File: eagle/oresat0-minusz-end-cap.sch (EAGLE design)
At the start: 30 parts, among them U1 LTC4305, U2 MMC5883MA, U3 MMC5883MA

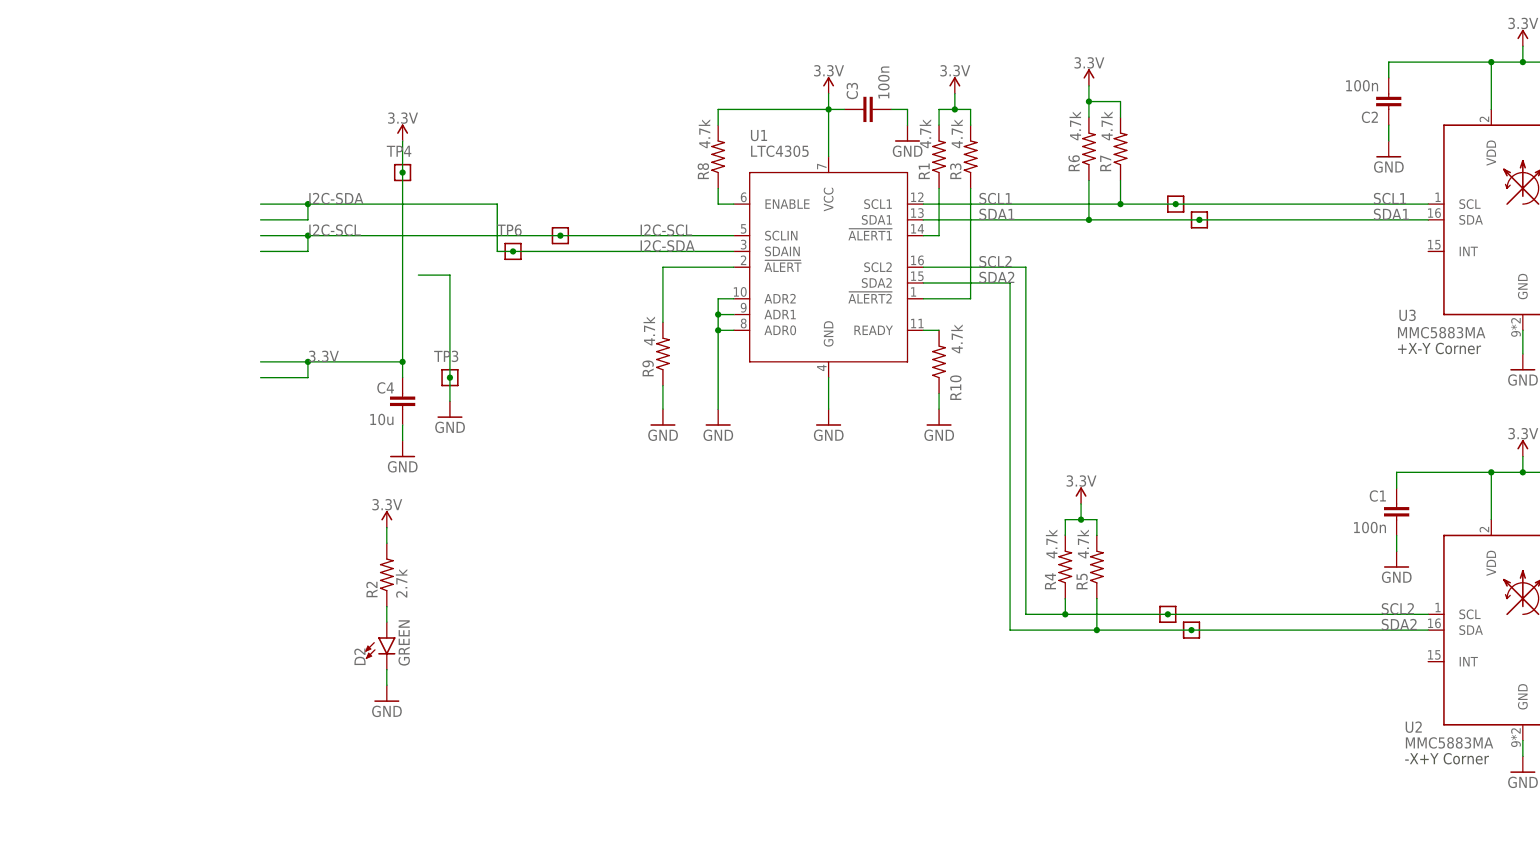
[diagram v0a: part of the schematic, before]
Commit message: Added connector to backplane. Added NP resistors connecting magnetometer interrupts to i2c buffer alert inputs. Moved traces out of bstop area, and moved components away from the backplane. Changed bus buffer i2c address. Added ground plane stitching, and fixed sharp edges on board outline.
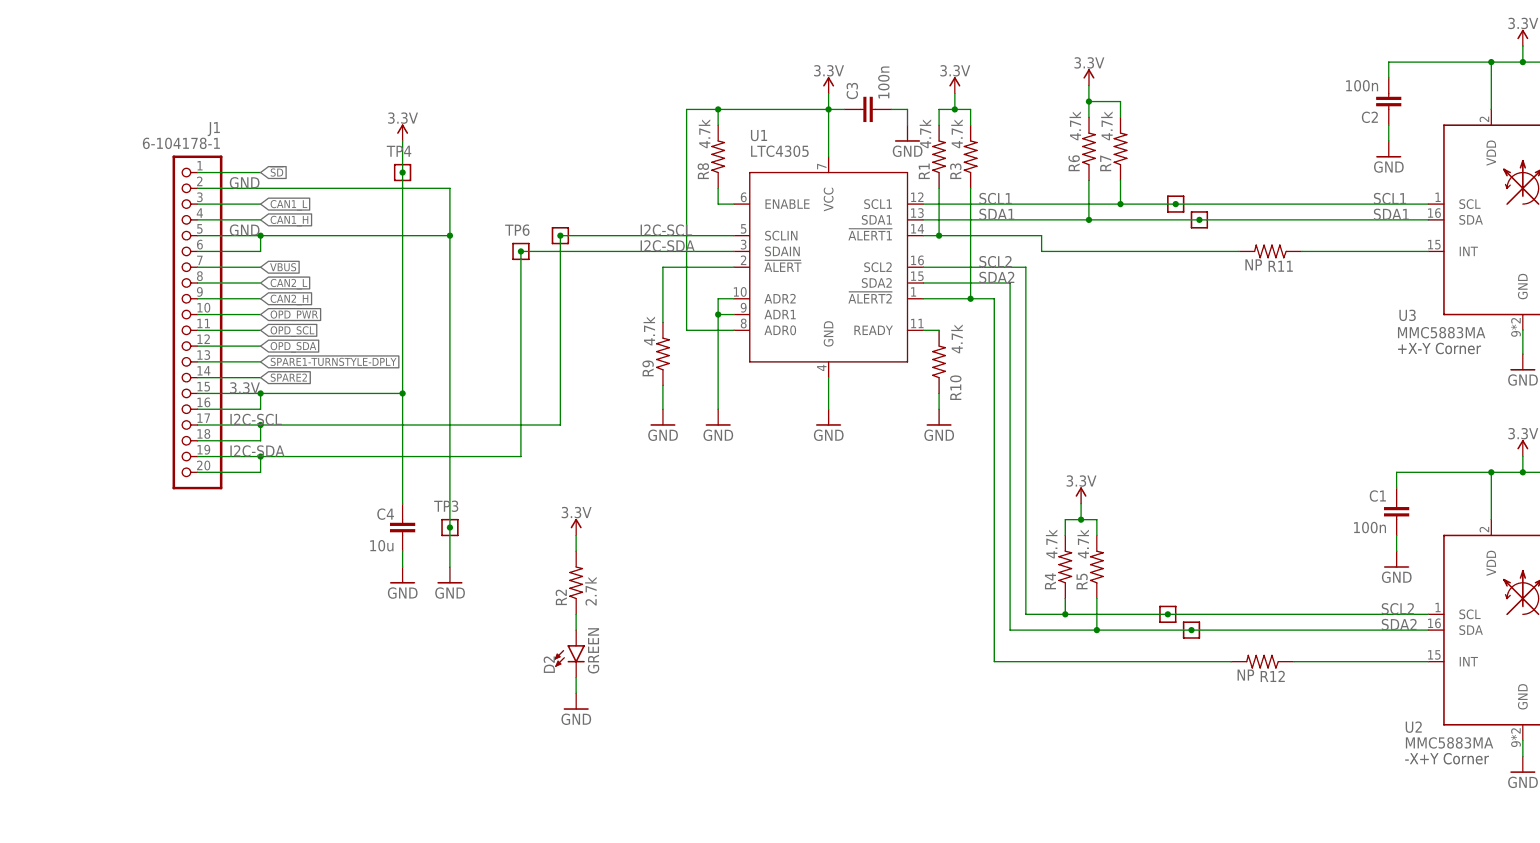
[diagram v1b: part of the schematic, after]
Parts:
- added J1: 6-104178-1, J-TE-6-104178-1-1.27mm-male-th:6-104178-1
- added R11, R12: NP, oresat-rcl:R-US_0603-B-NOSILK
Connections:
- new net !SD: J1.1
- new net CAN1_H: J1.4
- new net CAN1_L: J1.3
- new net CAN2_H: J1.9
- new net CAN2_L: J1.8
- new net N$10: R12.1, U2.INT
- new net N$8: R11.1, U3.INT
- new net OPD_PWR: J1.10
- new net OPD_SCL: J1.11
- new net OPD_SDA: J1.12
- new net SPARE1-TURNSTYLE-DPLY: J1.13
- new net SPARE2: J1.14
- new net VBUS: J1.7
- net 3.3V: now also J1.15, J1.16, U1.ADR0
- net GND: now also J1.2, J1.5, J1.6; no longer U1.ADR0
- net I2C-SCL: now also J1.17, J1.18
- net I2C-SDA: now also J1.19, J1.20
- net N$3: now also R11.2
- net N$4: now also R12.2
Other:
- moved on the sheet: C4, D2, R2, TP3, TP6

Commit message: v1.0 end caps for OreSat0!
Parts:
- added TP10, TP11, TP12, TP13, TP14, TP15, TP16, TP17, TP18, TP19, TP9: TEST-POINT-LARGE-SQUARE, oresat-misc:TEST-POINT-LARGE-SQUARE
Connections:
- net !SD: now also TP9.1
- net CAN1_H: now also TP11.1
- net CAN1_L: now also TP10.1
- net CAN2_H: now also TP14.1
- net CAN2_L: now also TP13.1
- net OPD_PWR: now also TP15.1
- net OPD_SCL: now also TP16.1
- net OPD_SDA: now also TP17.1
- net SPARE1-TURNSTYLE-DPLY: now also TP18.1
- net SPARE2: now also TP19.1
- net VBUS: now also TP12.1
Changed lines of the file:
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@@
 <?xml version="1.0" encoding="utf-8"?>
 <!DOCTYPE eagle SYSTEM "eagle.dtd">
-<eagle version="9.5.1">
+<eagle version="9.6.1">
 <drawing>
 <settings>
@@
 <setting verticaltext="up"/>
 </settings>
-<grid distance="0.05" unitdist="inch" unit="inch" style="lines" multiple="1" display="no" altdistance="0.01" altunitdist="inch" altunit="inch"/>
+<grid distance="0.1" unitdist="inch" unit="inch" style="lines" multiple="1" display="no" altdistance="0.01" altunitdist="inch" altunit="inch"/>
 <layers>
 <layer number="1" name="Top" color="4" fill="1" visible="no" active="no"/>
@@
 </part>
 <part name="J1" library="J-TE-6-104178-1-1.27mm-male-th" deviceset="6-104178-1" device=""/>
+<part name="TP9" library="oresat-misc" deviceset="TEST-POINT-LARGE-SQUARE" device=""/>
+<part name="TP10" library="oresat-misc" deviceset="TEST-POINT-LARGE-SQUARE" device=""/>
+<part name="TP11" library="oresat-misc" deviceset="TEST-POINT-LARGE-SQUARE" device=""/>
+<part name="TP12" library="oresat-misc" deviceset="TEST-POINT-LARGE-SQUARE" device=""/>
+<part name="TP13" library="oresat-misc" deviceset="TEST-POINT-LARGE-SQUARE" device=""/>
+<part name="TP14" library="oresat-misc" deviceset="TEST-POINT-LARGE-SQUARE" device=""/>
+<part name="TP15" library="oresat-misc" deviceset="TEST-POINT-LARGE-SQUARE" device=""/>
+<part name="TP16" library="oresat-misc" deviceset="TEST-POINT-LARGE-SQUARE" device=""/>
+<part name="TP17" library="oresat-misc" deviceset="TEST-POINT-LARGE-SQUARE" device=""/>
+<part name="TP18" library="oresat-misc" deviceset="TEST-POINT-LARGE-SQUARE" device=""/>
+<part name="TP19" library="oresat-misc" deviceset="TEST-POINT-LARGE-SQUARE" device=""/>
 </parts>
 <sheets>
@@
 <attribute name="VALUE" x="82.55" y="168.91" size="1.778" layer="96" rot="MR0"/>
 </instance>
+<instance part="TP9" gate="G$1" x="96.52" y="165.1" smashed="yes">
+<attribute name="NAME" x="99.06" y="165.1" size="1.27" layer="104"/>
+</instance>
+<instance part="TP10" gate="G$1" x="96.52" y="160.02" smashed="yes">
+<attribute name="NAME" x="99.06" y="160.02" size="1.27" layer="104"/>
+</instance>
+<instance part="TP11" gate="G$1" x="96.52" y="157.48" smashed="yes">
+<attribute name="NAME" x="99.06" y="157.48" size="1.27" layer="104"/>
+</instance>
+<instance part="TP12" gate="G$1" x="96.52" y="149.86" smashed="yes">
+<attribute name="NAME" x="99.06" y="149.86" size="1.27" layer="104"/>
+</instance>
+<instance part="TP13" gate="G$1" x="96.52" y="147.32" smashed="yes">
+<attribute name="NAME" x="99.06" y="147.32" size="1.27" layer="104"/>
+</instance>
+<instance part="TP14" gate="G$1" x="96.52" y="144.78" smashed="yes">
+<attribute name="NAME" x="99.06" y="144.78" size="1.27" layer="104"/>
+</instance>
+<instance part="TP15" gate="G$1" x="96.52" y="142.24" smashed="yes">
+<attribute name="NAME" x="99.06" y="142.24" size="1.27" layer="104"/>
+</instance>
+<instance part="TP16" gate="G$1" x="96.52" y="139.7" smashed="yes">
+<attribute name="NAME" x="99.06" y="139.7" size="1.27" layer="104"/>
+</instance>
+<instance part="TP17" gate="G$1" x="96.52" y="137.16" smashed="yes">
+<attribute name="NAME" x="99.06" y="137.16" size="1.27" layer="104"/>
+</instance>
+<instance part="TP18" gate="G$1" x="96.52" y="134.62" smashed="yes">
+<attribute name="NAME" x="99.06" y="134.62" size="1.27" layer="104"/>
+</instance>
+<instance part="TP19" gate="G$1" x="96.52" y="132.08" smashed="yes">
+<attribute name="NAME" x="99.06" y="132.08" size="1.27" layer="104"/>
+</instance>
 </instances>
 <busses>
@@
 <wire x1="78.74" y1="162.56" x2="119.38" y2="162.56" width="0.1524" layer="91"/>
 <pinref part="J1" gate="G$1" pin="5"/>
-<wire x1="78.74" y1="154.94" x2="88.9" y2="154.94" width="0.1524" layer="91"/>
+<wire x1="78.74" y1="154.94" x2="83.82" y2="154.94" width="0.1524" layer="91"/>
 <junction x="119.38" y="154.94"/>
 <pinref part="J1" gate="G$1" pin="6"/>
-<wire x1="88.9" y1="154.94" x2="119.38" y2="154.94" width="0.1524" layer="91"/>
-<wire x1="78.74" y1="152.4" x2="88.9" y2="152.4" width="0.1524" layer="91"/>
-<wire x1="88.9" y1="152.4" x2="88.9" y2="154.94" width="0.1524" layer="91"/>
-<junction x="88.9" y="154.94"/>
+<wire x1="83.82" y1="154.94" x2="119.38" y2="154.94" width="0.1524" layer="91"/>
+<wire x1="78.74" y1="152.4" x2="83.82" y2="152.4" width="0.1524" layer="91"/>
+<wire x1="83.82" y1="152.4" x2="83.82" y2="154.94" width="0.1524" layer="91"/>
+<junction x="83.82" y="154.94"/>
 <label x="83.82" y="162.56" size="1.778" layer="95"/>
 <label x="83.82" y="154.94" size="1.778" layer="95"/>
@@
 <segment>
 <pinref part="J1" gate="G$1" pin="1"/>
-<wire x1="78.74" y1="165.1" x2="88.9" y2="165.1" width="0.1524" layer="91"/>
-<label x="88.9" y="165.1" size="1.27" layer="95" xref="yes"/>
+<label x="83.82" y="165.1" size="1.27" layer="95"/>
+<pinref part="TP9" gate="G$1" pin="1"/>
+<wire x1="78.74" y1="165.1" x2="96.52" y2="165.1" width="0.1524" layer="91"/>
 </segment>
 </net>
@@
 <segment>
 <pinref part="J1" gate="G$1" pin="3"/>
-<wire x1="78.74" y1="160.02" x2="88.9" y2="160.02" width="0.1524" layer="91"/>
-<label x="88.9" y="160.02" size="1.27" layer="95" xref="yes"/>
+<label x="83.82" y="160.02" size="1.27" layer="95"/>
+<pinref part="TP10" gate="G$1" pin="1"/>
+<wire x1="78.74" y1="160.02" x2="96.52" y2="160.02" width="0.1524" layer="91"/>
 </segment>
 </net>
@@
 <segment>
 <pinref part="J1" gate="G$1" pin="4"/>
-<wire x1="78.74" y1="157.48" x2="88.9" y2="157.48" width="0.1524" layer="91"/>
-<label x="88.9" y="157.48" size="1.27" layer="95" xref="yes"/>
+<label x="83.82" y="157.48" size="1.27" layer="95"/>
+<pinref part="TP11" gate="G$1" pin="1"/>
+<wire x1="96.52" y1="157.48" x2="78.74" y2="157.48" width="0.1524" layer="91"/>
 </segment>
 </net>
@@
 <segment>
 <pinref part="J1" gate="G$1" pin="7"/>
-<wire x1="78.74" y1="149.86" x2="88.9" y2="149.86" width="0.1524" layer="91"/>
-<label x="88.9" y="149.86" size="1.27" layer="95" xref="yes"/>
+<label x="83.82" y="149.86" size="1.27" layer="95"/>
+<pinref part="TP12" gate="G$1" pin="1"/>
+<wire x1="78.74" y1="149.86" x2="96.52" y2="149.86" width="0.1524" layer="91"/>
 </segment>
 </net>
@@
 <segment>
 <pinref part="J1" gate="G$1" pin="8"/>
-<wire x1="78.74" y1="147.32" x2="88.9" y2="147.32" width="0.1524" layer="91"/>
-<label x="88.9" y="147.32" size="1.27" layer="95" xref="yes"/>
+<label x="83.82" y="147.32" size="1.27" layer="95"/>
+<pinref part="TP13" gate="G$1" pin="1"/>
+<wire x1="96.52" y1="147.32" x2="78.74" y2="147.32" width="0.1524" layer="91"/>
 </segment>
 </net>
@@
 <segment>
 <pinref part="J1" gate="G$1" pin="9"/>
-<wire x1="78.74" y1="144.78" x2="88.9" y2="144.78" width="0.1524" layer="91"/>
-<label x="88.9" y="144.78" size="1.27" layer="95" xref="yes"/>
+<label x="83.82" y="144.78" size="1.27" layer="95"/>
+<pinref part="TP14" gate="G$1" pin="1"/>
+<wire x1="78.74" y1="144.78" x2="96.52" y2="144.78" width="0.1524" layer="91"/>
 </segment>
 </net>
@@
 <segment>
 <pinref part="J1" gate="G$1" pin="10"/>
-<wire x1="78.74" y1="142.24" x2="88.9" y2="142.24" width="0.1524" layer="91"/>
-<label x="88.9" y="142.24" size="1.27" layer="95" xref="yes"/>
+<label x="83.82" y="142.24" size="1.27" layer="95"/>
+<pinref part="TP15" gate="G$1" pin="1"/>
+<wire x1="96.52" y1="142.24" x2="78.74" y2="142.24" width="0.1524" layer="91"/>
 </segment>
 </net>
@@
 <segment>
 <pinref part="J1" gate="G$1" pin="11"/>
-<wire x1="78.74" y1="139.7" x2="88.9" y2="139.7" width="0.1524" layer="91"/>
-<label x="88.9" y="139.7" size="1.27" layer="95" xref="yes"/>
+<label x="83.82" y="139.7" size="1.27" layer="95"/>
+<pinref part="TP16" gate="G$1" pin="1"/>
+<wire x1="78.74" y1="139.7" x2="96.52" y2="139.7" width="0.1524" layer="91"/>
 </segment>
 </net>
@@
 <segment>
 <pinref part="J1" gate="G$1" pin="12"/>
-<wire x1="78.74" y1="137.16" x2="88.9" y2="137.16" width="0.1524" layer="91"/>
-<label x="88.9" y="137.16" size="1.27" layer="95" xref="yes"/>
+<label x="83.82" y="137.16" size="1.27" layer="95"/>
+<pinref part="TP17" gate="G$1" pin="1"/>
+<wire x1="96.52" y1="137.16" x2="78.74" y2="137.16" width="0.1524" layer="91"/>
 </segment>
 </net>
@@
 <segment>
 <pinref part="J1" gate="G$1" pin="13"/>
-<wire x1="78.74" y1="134.62" x2="88.9" y2="134.62" width="0.1524" layer="91"/>
-<label x="88.9" y="134.62" size="1.27" layer="95" xref="yes"/>
+<label x="83.82" y="134.62" size="1.27" layer="95"/>
+<pinref part="TP18" gate="G$1" pin="1"/>
+<wire x1="78.74" y1="134.62" x2="96.52" y2="134.62" width="0.1524" layer="91"/>
 </segment>
 </net>
@@
 <segment>
 <pinref part="J1" gate="G$1" pin="14"/>
-<wire x1="78.74" y1="132.08" x2="88.9" y2="132.08" width="0.1524" layer="91"/>
-<label x="88.9" y="132.08" size="1.27" layer="95" xref="yes"/>
-</segment>
-</net>
+<label x="83.82" y="132.08" size="1.27" layer="95"/>
+<pinref part="TP19" gate="G$1" pin="1"/>
+<wire x1="96.52" y1="132.08" x2="78.74" y2="132.08" width="0.1524" layer="91"/>
+</segment>
+</net>

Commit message: Added BOMs and updated attributes for OreSat0 + and - Z end caps.
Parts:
- C1, C10, C2, C3, C7: DPN 1276-1001-1-ND -> 1276-CL10B104KB8NNNLCT-ND; MPN CL05B104KO5NNNC -> CL10B104KB8NNNL
- C12, C13, C4: DPN 1276-1001-1-ND -> 490-14461-1-ND; MFR Samsung -> Murata; MPN CL05B104KO5NNNC -> GRM188D71A106KA73D
- D2: DIS (none) -> Digi-Key; DPN (none) -> 511-1584-1-ND; MFR (none) -> Rohm; MPN (none) -> SML-E12M8WT86
- J1: DIS (none) -> Digi-Key; DPN (none) -> 952-3875-1-ND; MFR (none) -> TE Connectivity; MPN (none) -> 6-104178-1
- R1, R10, R3, R4, R5, R6, R7, R8, R9: DPN 1276-4275-1-ND -> A12969CT-ND; MFR Samsung -> TE Connectivity; MPN RC1005F6653CS -> CRGCQ0603F4K7
- R11, R12: DIS Digi-Key -> (none); DPN 1276-4275-1-ND -> (none); MFR Samsung -> (none); MPN RC1005F6653CS -> (none)
- R2: DPN 1276-4275-1-ND -> A129693CT-ND; MFR Samsung -> TE Connectivity; MPN RC1005F6653CS -> CRGCQ0603F2K7
- U1: DIS (none) -> Digi-Key; DPN (none) -> LTC4305IGN#PBF-ND; MFR (none) -> Analog; MPN (none) -> LTC4305IGN#PBF
- U2, U3: DIS (none) -> Digi-Key; DPN (none) -> 1267-1072-1-ND; MFR (none) -> Memsic; MPN (none) -> MMC5883MA

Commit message: New pretty OreSat0 end cap, now with updated launch provider.
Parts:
- added E1: ANT-2.4-CPA, ANT-Ethertonics-2.4-CPA:ANT-2.4-CPA
- added U$1: U.FL-R-SMA, J-HRS-U.FL-R-SMT-1(10)-M-RF:U.FL-R-SMA
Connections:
- new net N$9: E1.FEED, U$1.P$1
- net GND: now also U$1.P$2
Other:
- note added: "All caps are 0603 ceramic 10% X5R Vw>=16V unless marked"
- note added: "All resistors 0603 +/- 1% unless marked"
- note added: "Linx Technologies ANT-2.4-CPA S band patch antenna."
- note removed: "All caps are 0402 ceramic 10% X5R Vw>=16V unless marked"
- note removed: "All resistors 0402 +/- 1% unless marked"
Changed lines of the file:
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@@
 <setting verticaltext="up"/>
 </settings>
-<grid distance="0.1" unitdist="inch" unit="inch" style="lines" multiple="1" display="no" altdistance="0.01" altunitdist="inch" altunit="inch"/>
+<grid distance="0.05" unitdist="inch" unit="inch" style="lines" multiple="1" display="no" altdistance="0.01" altunitdist="inch" altunit="inch"/>
 <layers>
 <layer number="1" name="Top" color="4" fill="1" visible="no" active="no"/>
@@
 <part name="TP18" library="oresat-misc" deviceset="TEST-POINT-LARGE-SQUARE" device=""/>
 <part name="TP19" library="oresat-misc" deviceset="TEST-POINT-LARGE-SQUARE" device=""/>
+<part name="E1" library="ANT-Ethertonics-2.4-CPA" deviceset="ANT-2.4-CPA" device=""/>
+<part name="U$1" library="J-HRS-U.FL-R-SMT-1(10)-M-RF" deviceset="U.FL-R-SMA" device=""/>
+<part name="GND15" library="supply1" deviceset="GND" device=""/>
 </parts>
 <sheets>
@@
 <text x="341.63" y="26.67" size="3.81" layer="94">OreSat0 -Z End Cap</text>
 <text x="416.56" y="6.35" size="3.81" layer="94">2.0</text>
-<text x="11.43" y="5.08" size="1.778" layer="97">All resistors 0402 +/- 1% unless marked</text>
-<text x="11.43" y="2.54" size="1.778" layer="97">All caps are 0402 ceramic 10% X5R Vw&gt;=16V unless marked</text>
+<text x="11.43" y="5.08" size="1.778" layer="97">All resistors 0603 +/- 1% unless marked</text>
+<text x="11.43" y="2.54" size="1.778" layer="97">All caps are 0603 ceramic 10% X5R Vw&gt;=16V unless marked</text>
 <text x="273.05" y="69.85" size="1.778" layer="97">-X+Y Corner</text>
 <text x="271.78" y="135.89" size="1.778" layer="97">+X-Y Corner</text>
+<text x="203.2" y="232.41" size="1.778" layer="97">Linx Technologies ANT-2.4-CPA
+S band patch antenna.</text>
+<wire x1="157.48" y1="252.73" x2="157.48" y2="213.36" width="0.1524" layer="97"/>
+<wire x1="157.48" y1="213.36" x2="247.65" y2="213.36" width="0.1524" layer="97"/>
+<wire x1="247.65" y1="213.36" x2="247.65" y2="252.73" width="0.1524" layer="97"/>
+<wire x1="247.65" y1="252.73" x2="157.48" y2="252.73" width="0.1524" layer="97"/>
 </plain>
 <instances>
@@
 <instance part="TP19" gate="G$1" x="96.52" y="132.08" smashed="yes">
 <attribute name="NAME" x="99.06" y="132.08" size="1.27" layer="104"/>
+</instance>
+<instance part="E1" gate="G$1" x="186.69" y="240.03" smashed="yes">
+<attribute name="NAME" x="189.49041875" y="245.879590625" size="1.27291875" layer="95"/>
+<attribute name="VALUE" x="189.3632" y="243.84295" size="1.27295" layer="96"/>
+</instance>
+<instance part="U$1" gate="G$1" x="173.99" y="232.41" smashed="yes" rot="R90">
+<attribute name="NAME" x="163.83" y="227.33" size="1.778" layer="95" rot="R90"/>
+<attribute name="VALUE" x="167.64" y="227.33" size="1.778" layer="96" rot="R90"/>
+</instance>
+<instance part="GND15" gate="1" x="180.34" y="222.25" smashed="yes" rot="MR0">
+<attribute name="VALUE" x="182.88" y="219.71" size="1.778" layer="96" rot="MR0"/>
 </instance>
 </instances>
@@
 <wire x1="198.12" y1="129.54" x2="198.12" y2="127" width="0.1524" layer="91"/>
 </segment>
+<segment>
+<pinref part="U$1" gate="G$1" pin="P$2"/>
+<wire x1="179.07" y1="227.33" x2="180.34" y2="227.33" width="0.1524" layer="91"/>
+<pinref part="GND15" gate="1" pin="GND"/>
+<wire x1="180.34" y1="227.33" x2="180.34" y2="224.79" width="0.1524" layer="91"/>
+</segment>
 </net>
 <net name="3.3V" class="0">
@@
 </segment>
 </net>
+<net name="N$9" class="0">
+<segment>
+<pinref part="E1" gate="G$1" pin="FEED"/>
+<wire x1="186.69" y1="234.95" x2="186.69" y2="232.41" width="0.1524" layer="91"/>
+<pinref part="U$1" gate="G$1" pin="P$1"/>
+<wire x1="179.07" y1="232.41" x2="186.69" y2="232.41" width="0.1524" layer="91"/>
+</segment>
+</net>
 </nets>
 </sheet>
@@
 </drawing>
 <compatibility>
+<note version="6.3" minversion="6.2.2" severity="warning">
+Since Version 6.2.2 text objects can contain more than one line,
+which will not be processed correctly with this version.
+</note>
 <note version="8.2" severity="warning">
 Since Version 8.2, EAGLE supports online libraries. The ids
